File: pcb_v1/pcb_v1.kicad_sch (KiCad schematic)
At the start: 137 parts, among them U1 STM32WB55CGUx

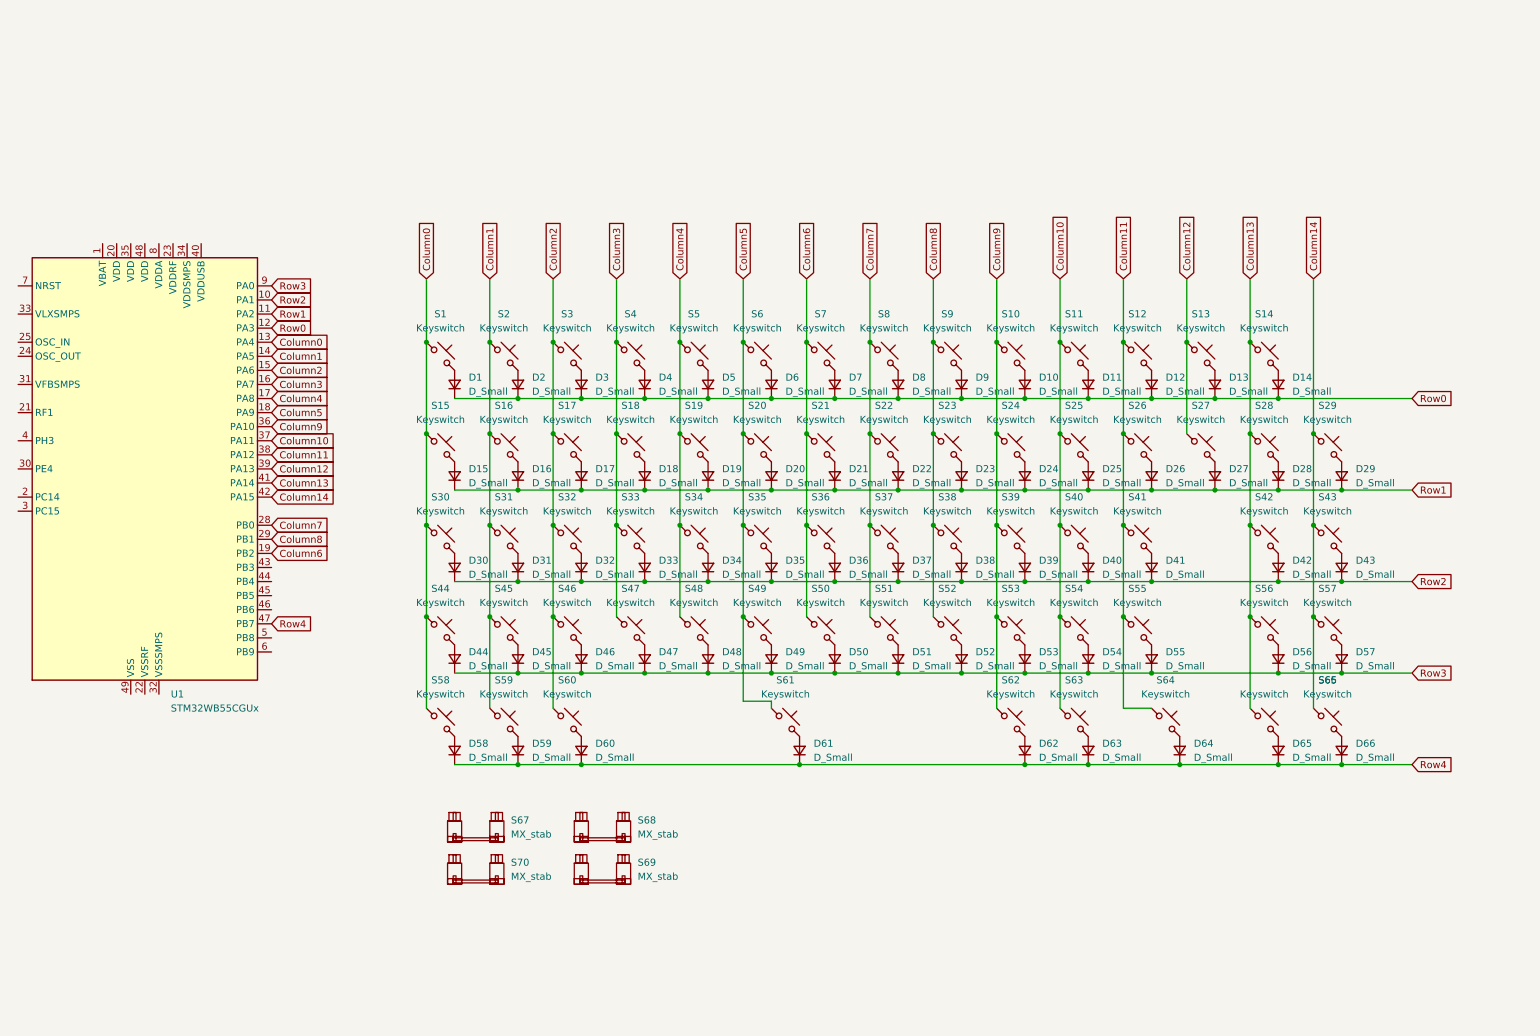
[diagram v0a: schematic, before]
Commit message: Added footprints for LEDs, Rotary Encoder
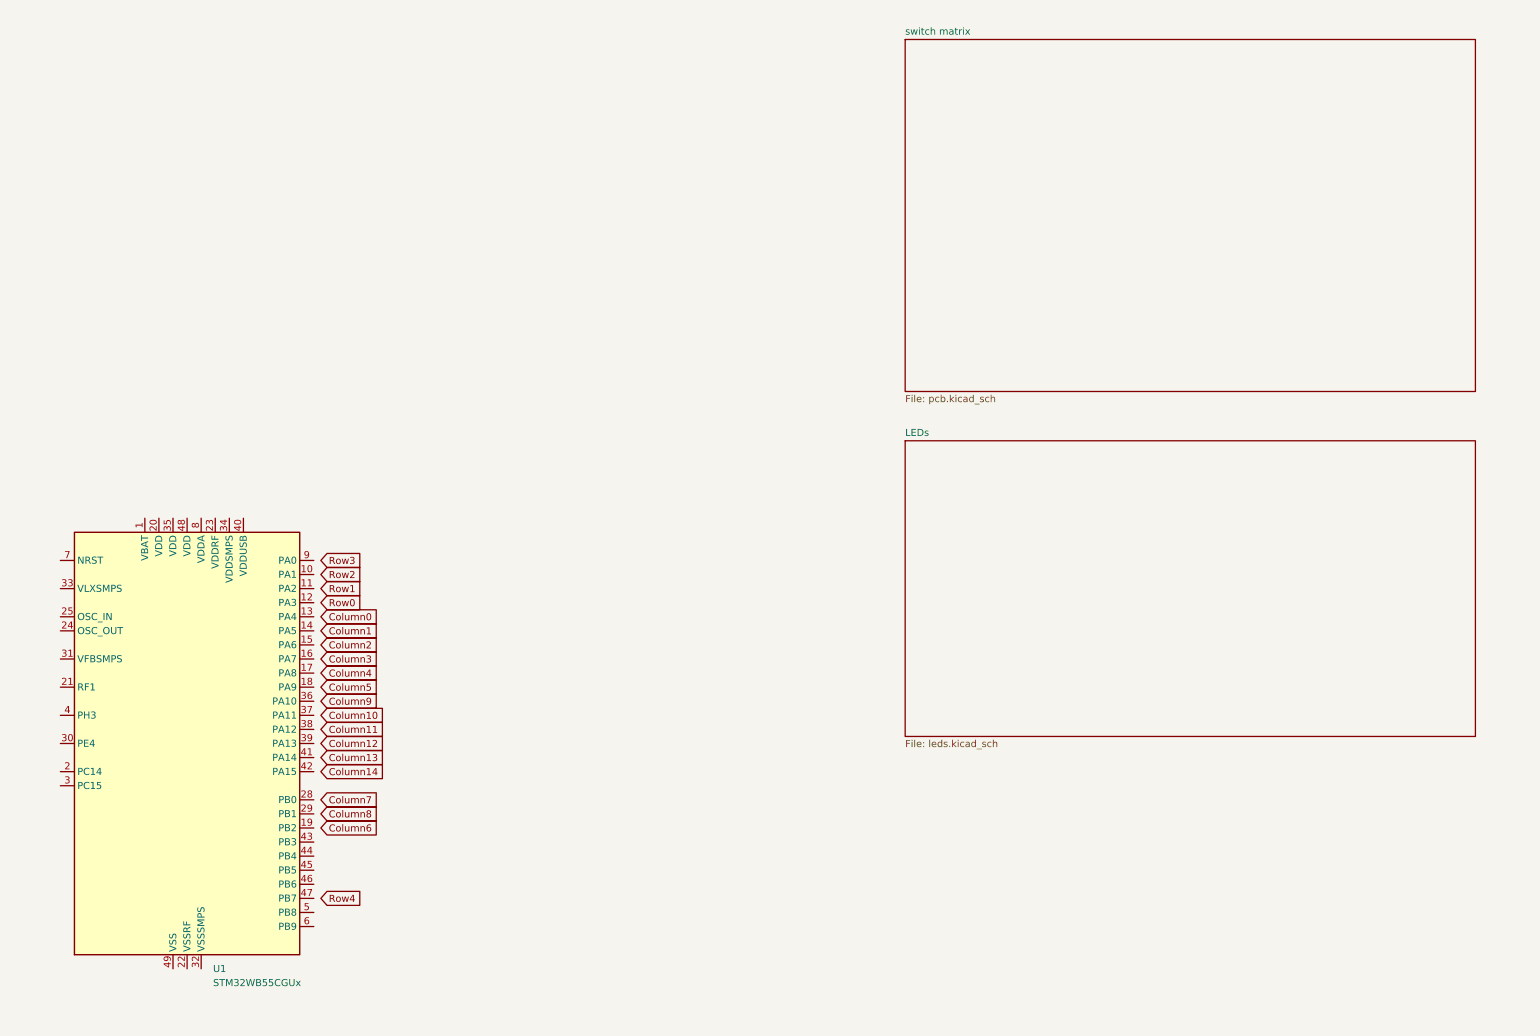
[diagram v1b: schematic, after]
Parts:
- removed D1, D10, D11, D12, D13, D14, D15, D16, D17, D18, D19, D2, D20, D21, D22, D23, D24, D25, D26, D27, D28, D29, D3, D30, D31, D32, D33, D34, D35, D36, D37, D38, D39, D4, D40, D41, D42, D43, D44, D45, D46, D47, D48, D49, D5, D50, D51, D52, D53, D54, D55, D56, D57, D58, D59, D6, D60, D61, D62, D63, D64, D65, D66, D7, D8, D9: D_Small, ScottoKeebs_Components:Diode_SOD-123, symbol Device:D_Small
- removed S1, S10, S11, S12, S13, S14, S16, S17, S18, S19, S2, S20, S21, S22, S23, S24, S25, S26, S27, S29, S3, S31, S32, S33, S34, S35, S36, S37, S38, S39, S4, S40, S41, S42, S43, S44, S45, S46, S47, S48, S49, S5, S50, S51, S52, S53, S54, S56, S57, S6, S61, S64, S65, S66, S7, S8, S9: Keyswitch, PCM_marbastlib-mx:SW_MX_HS_CPG151101S11_1u, symbol ScottoKeebs:Placeholder_Keyswitch
- removed S15, S28: Keyswitch, PCM_marbastlib-mx:SW_MX_HS_CPG151101S11_1.5u, symbol ScottoKeebs:Placeholder_Keyswitch
- removed S30, S55: Keyswitch, PCM_marbastlib-mx:SW_MX_HS_CPG151101S11_1.75u, symbol ScottoKeebs:Placeholder_Keyswitch
- removed S58, S59, S60, S62, S63: Keyswitch, PCM_marbastlib-mx:SW_MX_HS_CPG151101S11_1.25u, symbol ScottoKeebs:Placeholder_Keyswitch
- removed S67: MX_stab, PCM_marbastlib-mx:STAB_MX_P_2u, symbol PCM_marbastlib-mx:MX_stab
- removed S68, S69: MX_stab, PCM_marbastlib-mx:STAB_MX_2.25u, symbol PCM_marbastlib-mx:MX_stab
- removed S70: MX_stab, PCM_marbastlib-mx:STAB_MX_P_6.25u, symbol PCM_marbastlib-mx:MX_stab
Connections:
- net Column0: no longer U1.13 (PA4)
- net Column1: no longer U1.14 (PA5)
- net Column10: no longer U1.37 (PA11)
- net Column11: no longer U1.38 (PA12)
- net Column12: no longer U1.39 (PA13)
- net Column13: no longer U1.41 (PA14)
- net Column14: no longer U1.42 (PA15)
- net Column2: no longer U1.15 (PA6)
- net Column3: no longer U1.16 (PA7)
- net Column4: no longer U1.17 (PA8)
- net Column5: no longer U1.18 (PA9)
- net Column6: no longer U1.19 (PB2)
- net Column7: no longer U1.28 (PB0)
- net Column8: no longer U1.29 (PB1)
- net Column9: no longer U1.36 (PA10)
- net Row0: no longer U1.12 (PA3)
- net Row1: no longer U1.11 (PA2)
- net Row2: no longer U1.10 (PA1)
- net Row3: no longer U1.9 (PA0)
- net Row4: no longer U1.47 (PB7)
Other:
- added sheet LEDs (leds.kicad_sch)
- added sheet switch matrix (pcb.kicad_sch)
- moved on the sheet: U1

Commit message: Included Capacitors and JST connector in schematic. Upgraded MC to 69 pin version
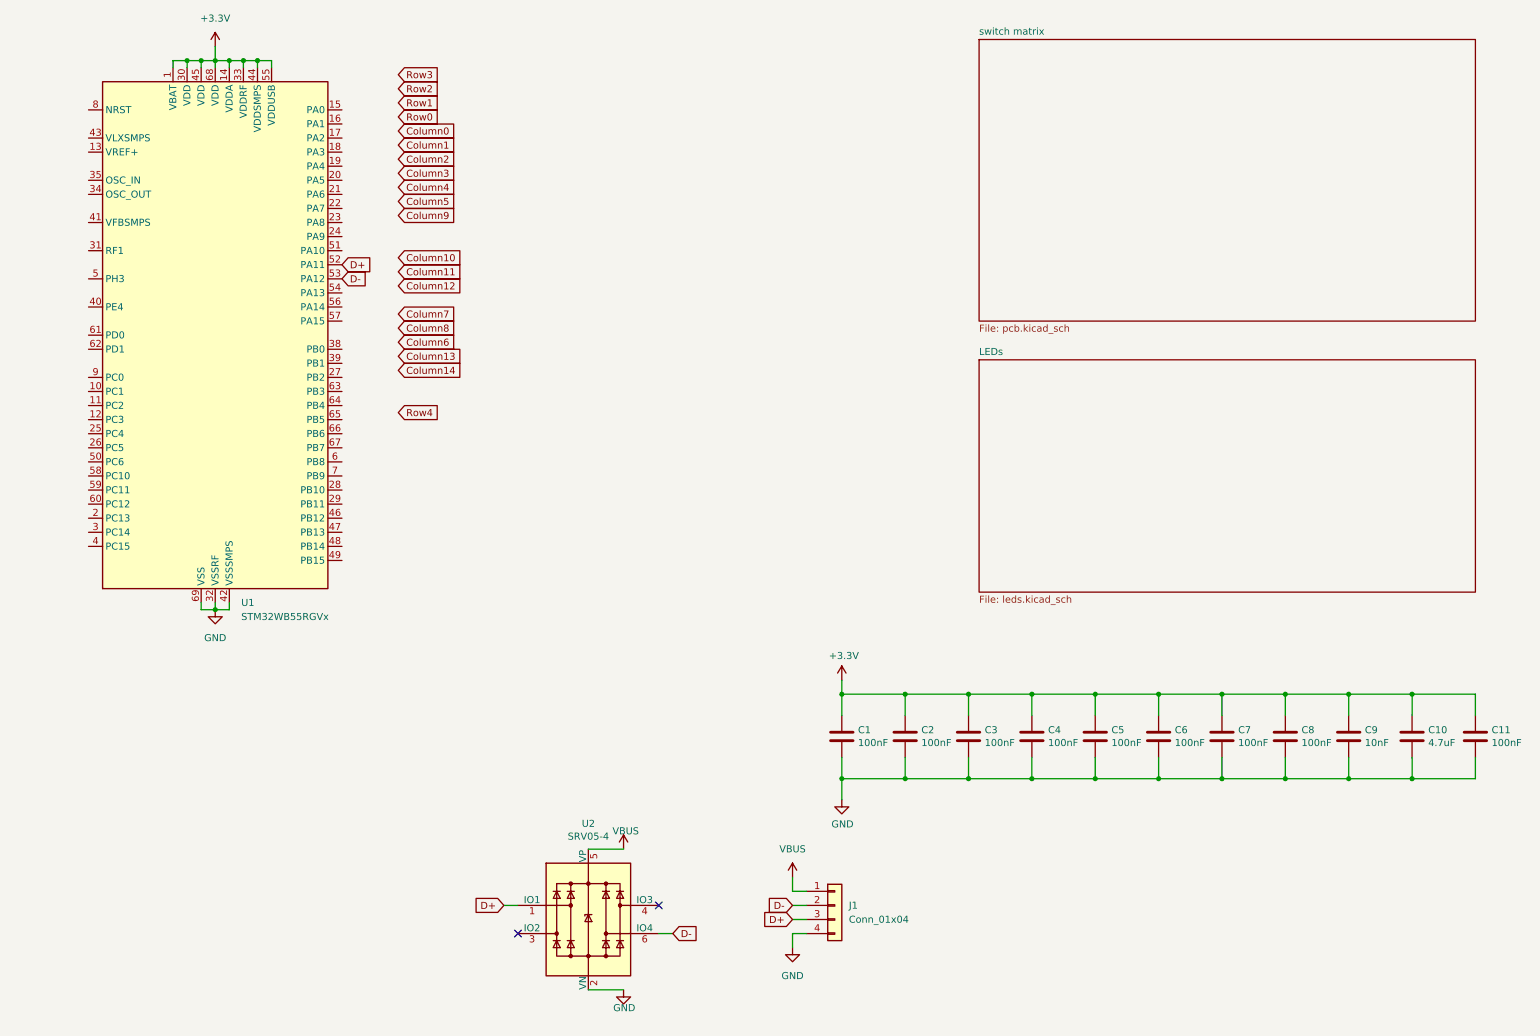
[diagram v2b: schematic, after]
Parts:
- removed U1: STM32WB55CGUx, Package_DFN_QFN:QFN-48-1EP_7x7mm_P0.5mm_EP5.6x5.6mm, symbol MCU_ST_STM32WB:STM32WB55CGUx
- added C1, C11, C2, C3, C4, C5, C6, C7, C8: 100nF, Capacitor_SMD:C_0805_2012Metric, symbol Device:C
- added C10: 4.7uF, Capacitor_SMD:C_0805_2012Metric, symbol Device:C
- added C9: 10nF, Capacitor_SMD:C_0805_2012Metric, symbol Device:C
- added J1: Conn_01x04, Connector_JST:JST_SH_SM04B-SRSS-TB_1x04-1MP_P1.00mm_Horizontal, symbol Connector_Generic:Conn_01x04
- added U1: STM32WB55RGVx, Package_DFN_QFN:QFN-68-1EP_8x8mm_P0.4mm_EP6.4x6.4mm, symbol MCU_ST_STM32WB:STM32WB55RGVx
- added U2: SRV05-4, Package_TO_SOT_SMD:SOT-23-6, symbol Power_Protection:SRV05-4
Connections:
- new net +3.3V: C1.1, C10.1, C11.1, C2.1, C3.1, C4.1, C5.1, C6.1, C7.1, C8.1, C9.1, U1.1 (VBAT), U1.14 (VDDA), U1.30 (VDD), U1.33 (VDDRF), U1.44 (VDDSMPS), U1.45 (VDD), U1.55 (VDDUSB), U1.68 (VDD)
- new net D+: J1.3 (Pin_3), U1.52 (PA11), U2.1 (IO1)
- new net D-: J1.2 (Pin_2), U1.53 (PA12), U2.6 (IO4)
- new net GND: C1.2, C10.2, C11.2, C2.2, C3.2, C4.2, C5.2, C6.2, C7.2, C8.2, C9.2, J1.4 (Pin_4), U1.32 (VSSRF), U1.42 (VSSSMPS), U1.69 (VSS), U2.2 (VN)
- new net VBUS: J1.1 (Pin_1), U2.5 (VP)
- no-connect marks 0 -> 2

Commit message: Added Flex Cuts
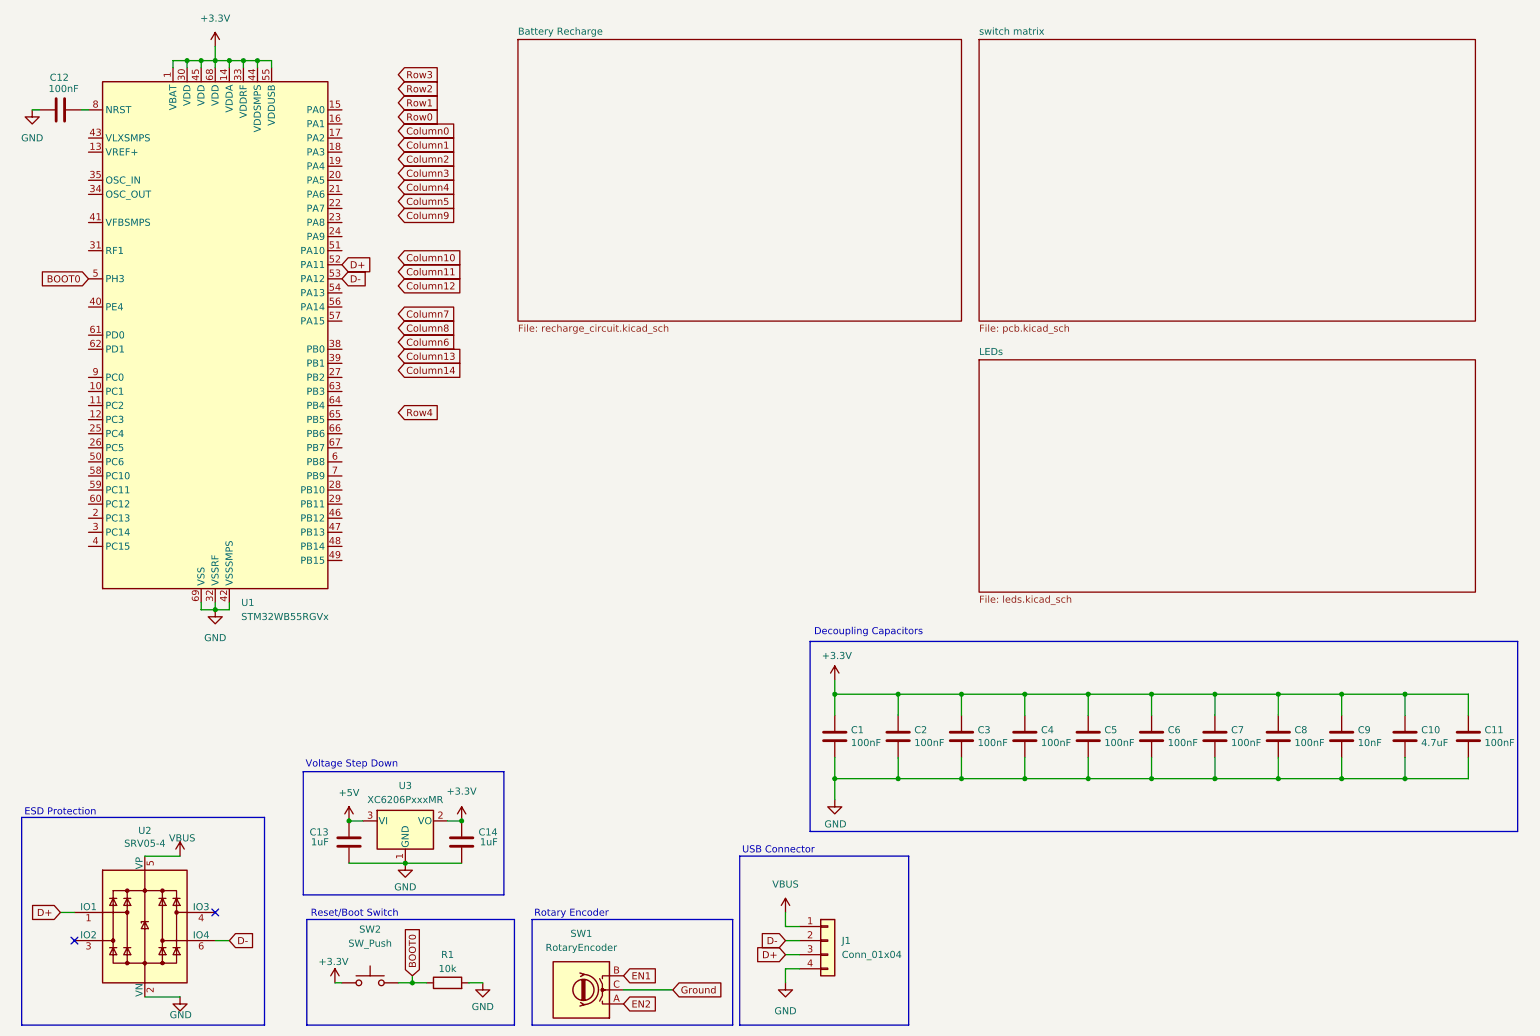
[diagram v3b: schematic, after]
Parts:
- added C12: 100nF, Capacitor_SMD:C_0805_2012Metric, symbol Device:C
- added C13, C14: 1uF, Capacitor_SMD:C_0805_2012Metric, symbol Device:C
- added R1: 10k, symbol ScottoKeebs:Placeholder_Resistor
- added SW1: RotaryEncoder, My_Footprints:EN05VS1212NHH, symbol Device:RotaryEncoder
- added SW2: SW_Push, symbol Switch:SW_Push
- added U3: XC6206PxxxMR, Package_TO_SOT_SMD:SOT-23-3, symbol Regulator_Linear:XC6206PxxxMR
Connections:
- net +3.3V: now also C14.1, SW2.1, U3.2 (VO)
- net GND: now also C12.1, C13.2, C14.2, R1.2, U3.1 (GND)
- net BOOT0: now reaches U1.5 (PH3)
- net BOOT0: now also R1.1, SW2.2
- net at U1.8 (NRST): now also C12.2
- new net +5V: C13.1, U3.3 (VI)
- new net EN1: SW1.B
- new net EN2: SW1.A
- new net Ground: SW1.C
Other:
- added sheet Battery Recharge (recharge_circuit.kicad_sch)
- note added: "Decoupling Capacitors"
- note added: "ESD Protection"
- note added: "Reset/Boot Switch"
- note added: "Rotary Encoder"
- note added: "USB Connector"
- note added: "Voltage Step Down"
- moved on the sheet: C1, C10, C11, C2, C3, C4, C5, C6, C7, C8, C9, J1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

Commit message: Re-drew PCB. Flipped to the correct orientation
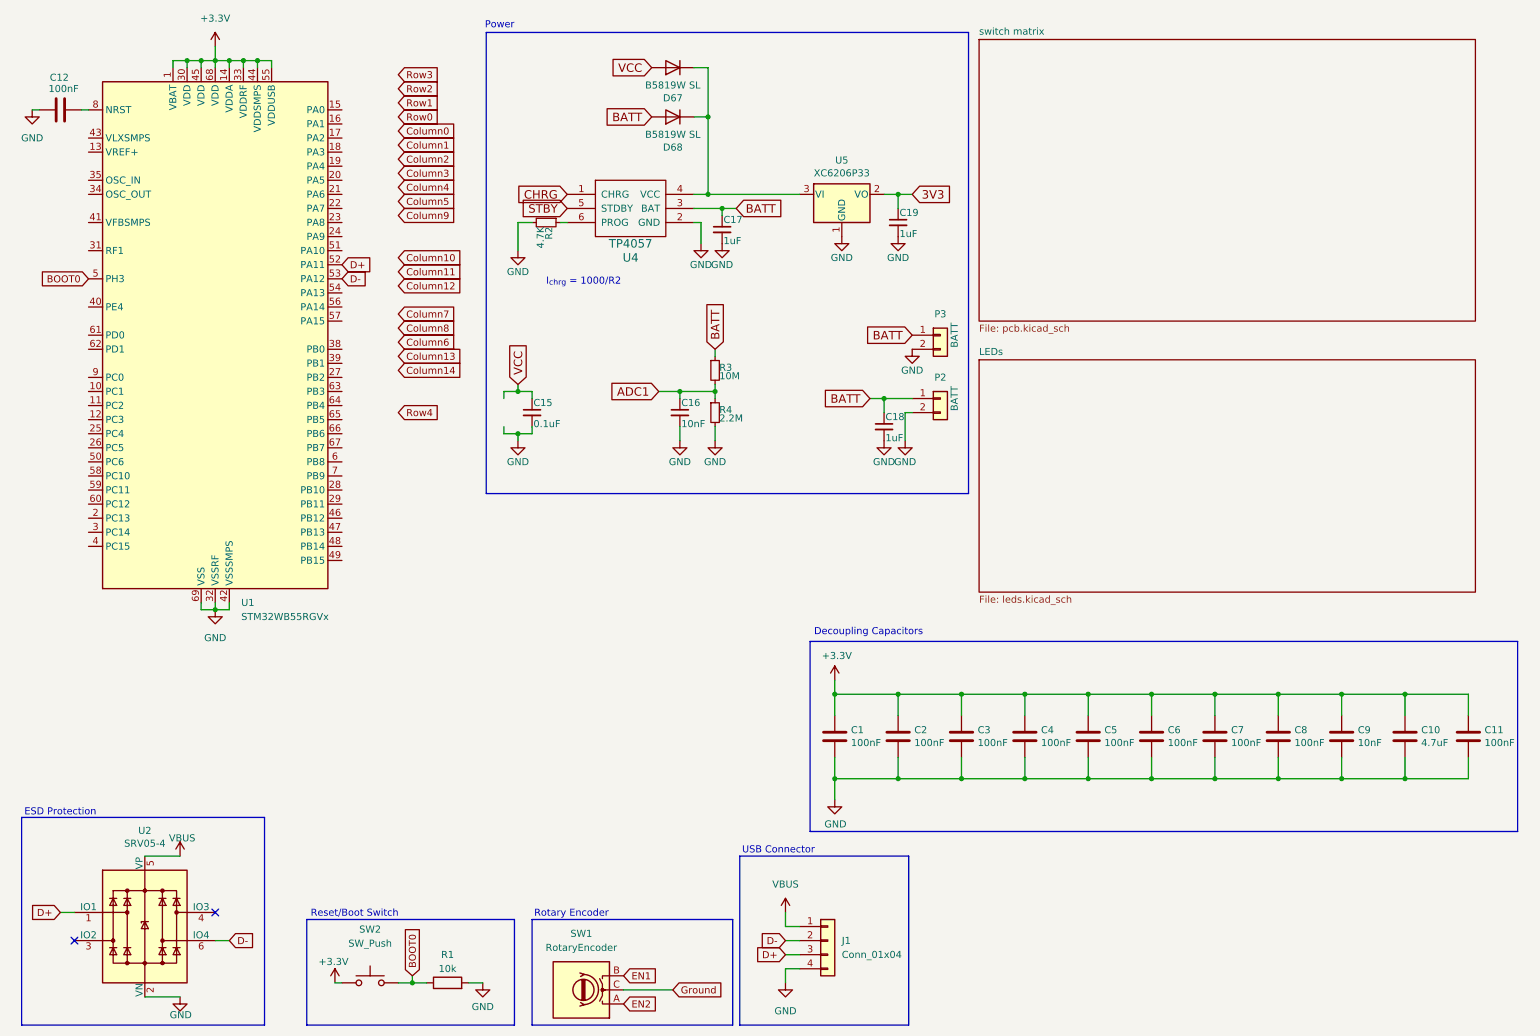
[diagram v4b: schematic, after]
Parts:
- removed C13, C14: 1uF, Capacitor_SMD:C_0805_2012Metric, symbol Device:C
- removed U3: XC6206PxxxMR, Package_TO_SOT_SMD:SOT-23-3, symbol Regulator_Linear:XC6206PxxxMR
- added C15: 0.1uF, Capacitor_SMD:C_0805_2012Metric, symbol Device:C_Small
- added C16: 10nF, Capacitor_SMD:C_0805_2012Metric, symbol Device:C_Small
- added C17, C18, C19: 1uF, Capacitor_SMD:C_0805_2012Metric, symbol Device:C_Small
- added D67, D68: B5819W SL, Diode_SMD:D_SOD-123, symbol Device:D
- added P2: BATT, Connector_PinHeader_2.54mm:PinHeader_1x02_P2.54mm_Vertical, symbol Connector_Generic:Conn_01x02
- added P3: BATT, Connector_PinSocket_2.00mm:PinSocket_1x02_P2.00mm_Vertical, symbol Connector_Generic:Conn_01x02
- added R2: 4.7K, Resistor_SMD:R_0805_2012Metric, symbol Device:R_Small
- added R3: 10M, Resistor_SMD:R_0805_2012Metric, symbol Device:R_Small
- added R4: 2.2M, Resistor_SMD:R_0805_2012Metric, symbol Device:R_Small
- added U4: TP4057, Package_TO_SOT_SMD:SOT-23-6, symbol custom:TP4057
- added U5: XC6206P33, Package_TO_SOT_SMD:SOT-23, symbol Regulator_Linear:AP2127N-3.0
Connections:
- net GND: now also C15.2, C16.2, C17.2, C18.2, C19.2, P2.2 (Pin_2), P3.2 (Pin_2), R2.2, R4.2, U4.2 (GND), U5.1 (GND)
- new net: R2.1, U4.6 (PROG)
- new net: D67.1 (K), D68.1 (K), U4.4 (VCC), U5.3 (VI)
- new net 3V3: C19.1, U5.2 (VO)
- new net ADC1: C16.1, R3.2, R4.1
- new net BATT: C17.1, C18.1, D68.2 (A), P2.1 (Pin_1), P3.1 (Pin_1), R3.1, U4.3 (BAT)
- new net CHRG: U4.1 (CHRG)
- new net STBY: U4.5 (STDBY)
- new net VCC: C15.1, D67.2 (A)
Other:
- removed sheet Battery Recharge
- note added: "I_{chrg} = 1000/R2"
- note added: "Power"
- note removed: "Voltage Step Down"
